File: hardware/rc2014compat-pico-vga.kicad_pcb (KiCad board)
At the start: 2 copper layers, 99.1 x 49.9 mm, 3 parts

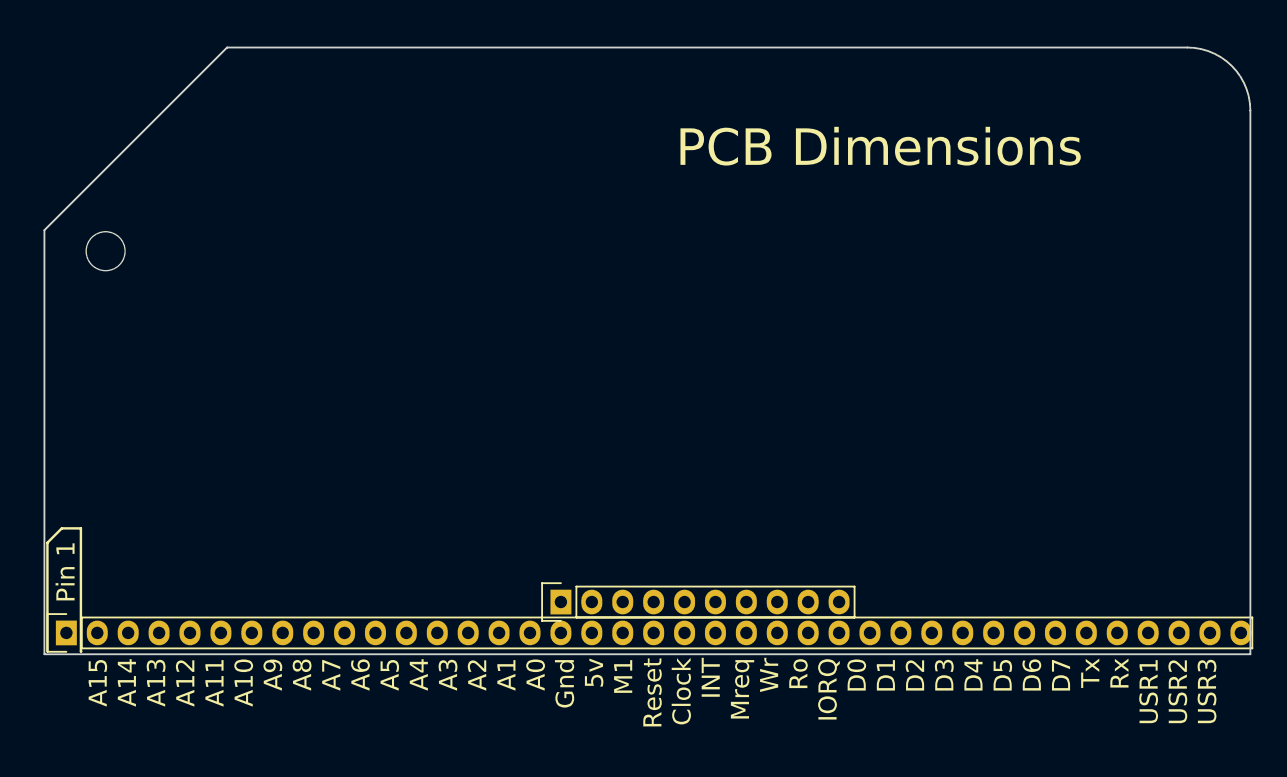
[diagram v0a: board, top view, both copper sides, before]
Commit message: hardware: pcb routing complete
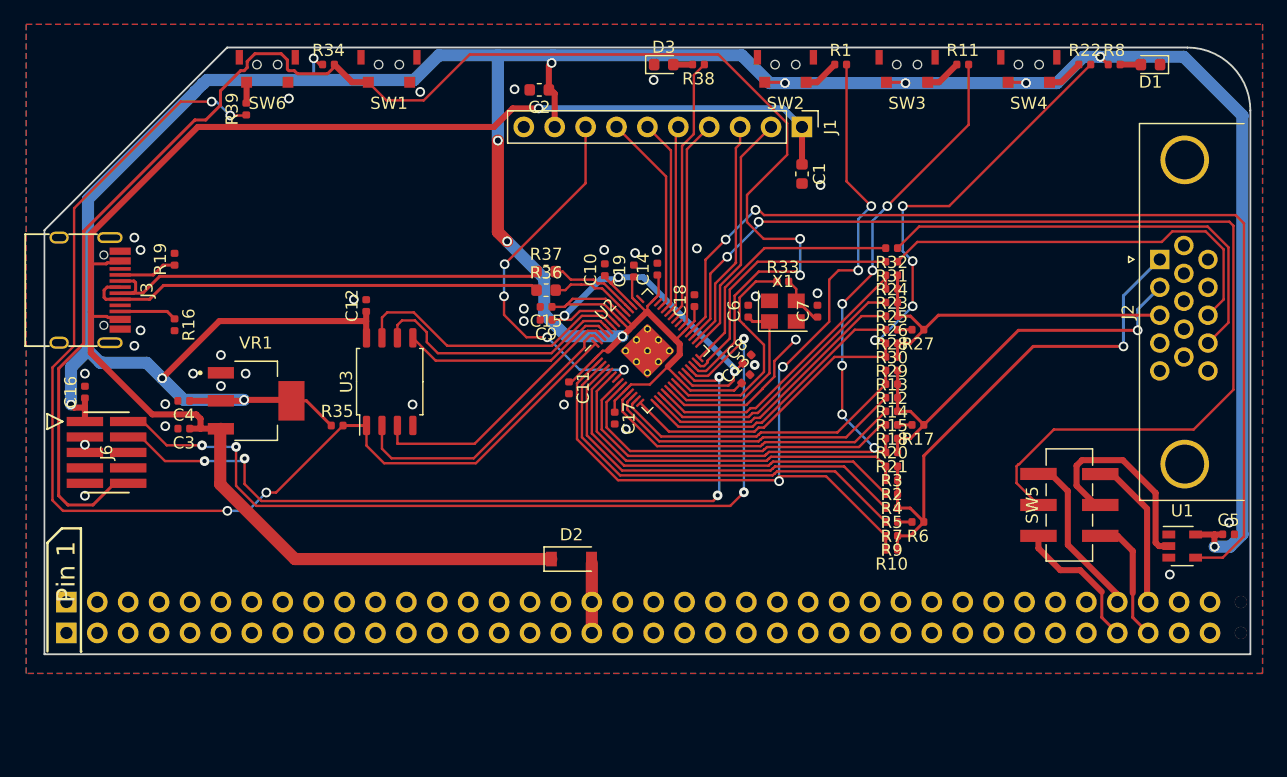
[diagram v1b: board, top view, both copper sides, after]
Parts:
- removed ?: , Mounting_Holes:MountingHole_3.2mm_M3
- removed ?: , Pin_Headers:Pin_Header_Straight_1x40
- removed ?: , Pin_Headers:Pin_Header_Straight_1x10
- added C1: 10uF,10V,X5R, tom-passives:C_0603_1608Metric, F.Cu at (216.2, 113.9)
- added C10: 10uF,6.3V,X5R, tom-passives:C_0402_1005Metric, F.Cu at (199.9, 121.8)
- added C11: 100nF,16V,X7R, tom-passives:C_0402_1005Metric, F.Cu at (197.0, 131.5)
- added C12: 100nF,16V,X7R, tom-passives:C_0402_1005Metric, F.Cu at (180.3, 124.7)
- added C13: 100nF,16V,X7R, tom-passives:C_0402_1005Metric, F.Cu at (211.5, 130.7)
- added C14: 100nF,16V,X7R, tom-passives:C_0402_1005Metric, F.Cu at (204.3, 121.7)
- added C15: 100nF,16V,X7R, tom-passives:C_0402_1005Metric, F.Cu at (195.1, 124.8)
- added C16: 100nF,16V,X7R, tom-passives:C_0402_1005Metric, F.Cu at (157.2, 131.8)
- added C17: 100nF,16V,X7R, tom-passives:C_0402_1005Metric, F.Cu at (200.8, 134.0)
- added C18: 100nF,16V,X7R, tom-passives:C_0402_1005Metric, F.Cu at (207.3, 124.3)
- added C19: 2.2uF,6.3V,X5R, tom-passives:C_0402_1005Metric, F.Cu at (202.3, 121.9)
- added C2: 10uF,10V,X5R, tom-passives:C_0603_1608Metric, F.Cu at (194.6, 107.0)
- added C3: 1uF,25V,X5R, tom-passives:C_0402_1005Metric, F.Cu at (165.4, 134.8)
- added C4: 1uF,25V,X5R, tom-passives:C_0402_1005Metric, F.Cu at (165.4, 132.5)
- added C5: 100nF,16V,X7R, tom-passives:C_0402_1005Metric, F.Cu at (251.2, 143.5)
- added C6: 20pF,50V,C0G, tom-passives:C_0402_1005Metric, F.Cu at (211.7, 125.2)
- added C7: 20pF,50V,C0G, tom-passives:C_0402_1005Metric, F.Cu at (217.4, 125.2)
- added C8: 100nF,16V,X7R, tom-passives:C_0402_1005Metric, F.Cu at (211.6, 129.1)
- added C9: 100nF,16V,X7R, tom-passives:C_0402_1005Metric, F.Cu at (195.1, 125.9)
- added D1: LED, tom-opto:LED_0603_1608Metric, F.Cu at (244.8, 104.9)
- added D2: 1N5817, tom-semiconductors:D_SOD-123, F.Cu at (197.2, 145.5)
- added D3: LED, tom-opto:LED_0603_1608Metric, F.Cu at (204.8, 104.9)
- added J1: Conn_01x10_Female, tom-connectors:PinHeader_1x10_P2.54mm_Vertical, F.Cu at (216.1, 110.0)
- added J2: DB15_Female_HighDensity_MountingHoles, tom-connectors:DSUB-15-HD_Female_Horizontal_P2.29x1.98mm_EdgePinOffset3.03mm_Housed_MountingHolesOffset4.94mm, F.Cu at (245.6, 120.9)
- added J3: USB_C_Receptacle_USB2.0, tom-connectors:USB_C_Receptacle_GT-USB-7010, F.Cu at (157.0, 123.4)
- added J4: RC2014-ENH, tom-connectors:PinHeader_1x39_P2.54mm_Horizontal, B.Cu at (155.7, 149.1)
- added J5: RC2014-STD, tom-connectors:PinHeader_1x39_P2.54mm_Horizontal, B.Cu at (155.7, 151.6)
- added J6: Conn_02x05_SWD, tom-connectors:FTSH-105-01-F-DV-K, F.Cu at (159.0, 136.8)
- added R1: 1k, tom-passives:R_0402_1005Metric, F.Cu at (219.3, 104.9)
- added R10: 12k, tom-passives:R_0402_1005Metric, F.Cu at (223.5, 144.8)
- added R11: 1k, tom-passives:R_0402_1005Metric, F.Cu at (229.4, 104.9)
- added R12: 1k, tom-passives:R_0402_1005Metric, F.Cu at (223.5, 131.2)
- added R13: 1k, tom-passives:R_0402_1005Metric, F.Cu at (223.5, 130.0)
- added R14: 1k, tom-passives:R_0402_1005Metric, F.Cu at (223.5, 132.3)
- added R15: 2k, tom-passives:R_0402_1005Metric, F.Cu at (223.5, 133.4)
- added R16: 5.1k, tom-passives:R_0402_1005Metric, F.Cu at (164.6, 126.3)
- added R17: 2k, tom-passives:R_0402_1005Metric, F.Cu at (225.7, 134.5)
- added R18: 2k, tom-passives:R_0402_1005Metric, F.Cu at (223.5, 134.5)
- added R19: 5.1k, tom-passives:R_0402_1005Metric, F.Cu at (164.6, 120.9)
- added R2: 1k, tom-passives:R_0402_1005Metric, F.Cu at (223.5, 139.1)
- added R20: 24k, tom-passives:R_0402_1005Metric, F.Cu at (223.5, 135.6)
- added R21: 12k, tom-passives:R_0402_1005Metric, F.Cu at (223.5, 136.8)
- added R22: 1k, tom-passives:R_0402_1005Metric, F.Cu at (239.4, 104.9)
- added R23: 1k, tom-passives:R_0402_1005Metric, F.Cu at (223.5, 123.3)
- added R24: 1k, tom-passives:R_0402_1005Metric, F.Cu at (223.5, 122.2)
- added R25: 1k, tom-passives:R_0402_1005Metric, F.Cu at (223.5, 124.5)
- added R26: 2k, tom-passives:R_0402_1005Metric, F.Cu at (223.5, 125.6)
- added R27: 2k, tom-passives:R_0402_1005Metric, F.Cu at (225.7, 126.7)
- added R28: 2k, tom-passives:R_0402_1005Metric, F.Cu at (223.5, 126.7)
- added R29: 24k, tom-passives:R_0402_1005Metric, F.Cu at (223.5, 128.9)
- added R3: 1k, tom-passives:R_0402_1005Metric, F.Cu at (223.5, 137.9)
- added R30: 12k, tom-passives:R_0402_1005Metric, F.Cu at (223.5, 127.8)
- added R31: 47, tom-passives:R_0402_1005Metric, F.Cu at (223.5, 121.1)
- added R32: 47, tom-passives:R_0402_1005Metric, F.Cu at (223.5, 120.0)
- added R33: 1k, tom-passives:R_0402_1005Metric, F.Cu at (214.6, 122.7)
- added R34: 10k, tom-passives:R_0402_1005Metric, F.Cu at (177.2, 104.9)
- added R35: 10k, tom-passives:R_0402_1005Metric, F.Cu at (178.0, 134.6)
- added R36: 27, tom-passives:R_0603_1608Metric, F.Cu at (195.1, 123.4)
- added R37: 27, tom-passives:R_0603_1608Metric, F.Cu at (195.1, 121.9)
- added R38: 470, tom-passives:R_0402_1005Metric, F.Cu at (207.6, 104.9)
- added R39: 1k, tom-passives:R_0402_1005Metric, F.Cu at (170.5, 108.6)
- added R4: 1k, tom-passives:R_0402_1005Metric, F.Cu at (223.5, 140.2)
- added R5: 2k, tom-passives:R_0402_1005Metric, F.Cu at (223.5, 141.4)
- added R6: 2k, tom-passives:R_0402_1005Metric, F.Cu at (225.7, 142.5)
- added R7: 2k, tom-passives:R_0402_1005Metric, F.Cu at (223.5, 142.5)
- added R8: 470, tom-passives:R_0402_1005Metric, F.Cu at (241.8, 104.9)
- added R9: 24k, tom-passives:R_0402_1005Metric, F.Cu at (223.5, 143.6)
- added SW1: C319395, tom-mechanical:SW_SPST_SMD_SIDE_C319395, F.Cu at (182.2, 104.9)
- added SW2: C319395, tom-mechanical:SW_SPST_SMD_SIDE_C319395, F.Cu at (214.8, 104.9)
- added SW3: C319395, tom-mechanical:SW_SPST_SMD_SIDE_C319395, F.Cu at (224.8, 104.9)
- added SW4: C319395, tom-mechanical:SW_SPST_SMD_SIDE_C319395, F.Cu at (234.8, 104.9)
- added SW5: SW_DPDT_x2, tom-mechanical:SW_DPDT_SMD, F.Cu at (238.1, 141.1)
- added SW6: Switch_SW_Push, tom-mechanical:SW_SPST_SMD_SIDE_C319395, F.Cu at (172.2, 104.9)
- added U1: 74LVC1G125, tom-semiconductors:SOT-23-5, F.Cu at (247.4, 144.5)
- added U2: RP2040, tom-semiconductors:RP2040-QFN-56, F.Cu at (203.4, 128.4)
- added U3: W25Q128JVS, tom-semiconductors:SOIC-8_5.23x5.23mm_P1.27mm, F.Cu at (182.3, 131.0)
- added VR1: LM1117MPX-3.3, tom-semiconductors:VREG_LM1117MPX-3.3, F.Cu at (171.3, 132.5)
- added X1: 12MHz, tom-passives:Crystal_SMD_3225-4Pin_3.2x2.5mm, F.Cu at (214.6, 125.2)
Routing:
- net +3.3V: track 0.00 -> 309.3 mm, vias 0 -> 13
- net /RP2040/~{RESET}: track 0.00 -> 132.0 mm, vias 0 -> 2
- net +5V: track 0.00 -> 130.1 mm, vias 0 -> 1
- net /RP2040/QSPI_SS: track 0.00 -> 97.1 mm, vias 0 -> 4
- net /UART_TX: track 0.00 -> 88.7 mm, vias 0 -> 2
- net /UART_RX_3.3: track 0.00 -> 83.4 mm, vias 0 -> 2
- net /RP2040/GPIO0: track 0.00 -> 76.8 mm, vias 0 -> 4
- net /RP2040/SWD: track 0.00 -> 74.5 mm, vias 0 -> 4
- net /RP2040/GPIO6: track 0.00 -> 67.2 mm, vias 0 -> 6
- net /RP2040/SWCLK: track 0.00 -> 65.2 mm, vias 0 -> 4
- net /RP2040/GPIO11: track 0.00 -> 58.9 mm, vias 0 -> 4
- net /VGA_R: track 0.00 -> 43.8 mm, vias 0 -> 1
- net /USB_P: track 0.00 -> 38.3 mm
- net /USB_N: track 0.00 -> 37.4 mm
- net /VGA_VS: track 0.00 -> 37.2 mm
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- added copper zone on B.Cu, net GND
- added copper zone on F.Cu, net GND
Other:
- rule pad_to_mask_clearance: 0.2 -> 0
- board text removed: "135 deg"
- board text removed: "5.1mm radius"
- board text removed: "A15 A14 A13 A12 A11 A10 A9 A8 A7 A6 A5 A4 A3 A2 A1 A0 Gnd 5v M1 Reset Clock INT Mreq Wr Ro IORQ D0 D1 D2 D3 D4 D5 D6 D7 Tx Rx USR1 USR2 USR3"
- board text removed: "Gnd 5v RFSH Page Clock 2 BUSACK HALT BUSRQ WAIT NMI D8 D9 D10 D11 D12 D13 D14 D15 Tx2 Rx2 USR5 USR6 USR7"
- board text removed: "M3 Mounting Hole"
- board text removed: "PCB Dimensions"

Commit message: hardware: Sep2022 as submitted
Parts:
- moved R11 11.2 mm to (223.2, 114.2), turned to -90 degrees
- moved C2 4.29 mm to (194.5, 111.3)
- moved J1 4.00 mm to (216.1, 114.0)
- moved C1 3.83 mm to (217.9, 110.5), turned to 90 degrees
- moved C12 3.38 mm to (178.2, 127.4), turned to 180 degrees
- moved R39 1.47 mm to (169.0, 108.6)
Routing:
- net /RP2040/GPIO6: track 67.2 -> 54.6 mm
- net +3.3V: track 309.3 -> 315.2 mm, vias 13 -> 12
- net Net-(R11-Pad1): track 2.99 -> 8.78 mm
- net /GPIO5: track 30.9 -> 26.3 mm
- net +5V: track 130.1 -> 134.5 mm
- net /GPIO18: track 20.3 -> 16.1 mm
- net /GPIO28: track 16.5 -> 12.5 mm
- net /GPIO22: track 17.3 -> 13.3 mm
- net /GPIO27: track 16.0 -> 12.0 mm
- net /GPIO19: track 19.0 -> 15.0 mm
- net /GPIO26: track 15.3 -> 11.6 mm
- net /RP2040/~{RESET}: track 132.0 -> 133.3 mm
- net /RP2040/SWD: track 74.5 -> 73.3 mm
- net /RP2040/SWCLK: track 65.2 -> 64.2 mm
- net /RP2040/QSPI_SS: track 97.1 -> 96.2 mm
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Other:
- board text added: "@TomKeddie - Designed for RC2014 - Sep2022"
- board text added: "A"
- board text added: "B"
- board text added: "BOOT"
- board text added: "C"
- board text added: "GPIO25"
- board text added: "PWR"
- board text added: "Pi Pico VGA Terminal Compatible"
- board text added: "RESET"
